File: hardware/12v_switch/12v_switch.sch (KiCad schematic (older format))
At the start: 51 parts, among them J1 MOLEX_0530470810, M1 SCREW_6-32_POWER, M11 SCREW_6-32_POWER, M12 SCREW_6-32_POWER, M13 SCREW_6-32_POWER, M14 SCREW_6-32_POWER, M19 SCREW_6-32_NORMAL, M2 SCREW_6-32_POWER, M20 SCREW_6-32_NORMAL, M21 SCREW_6-32_NORMAL, M22 SCREW_6-32_NORMAL, M3 SCREW_6-32_POWER, M4 SCREW_6-32_POWER, M5 SCREW_6-32_POWER, M6 SCREW_6-32_POWER, Q1 INFINEON_IRF7470TRPBF, Q2 INFINEON_IRF7470TRPBF, Q3 INFINEON_IRF7470TRPBF, Q4 INFINEON_IRF7470TRPBF, U1 TI_LM5111-1MX_NOPB, U2 TI_LM5111-1MX_NOPB, U3 TI_LM22680QMRE-ADJ

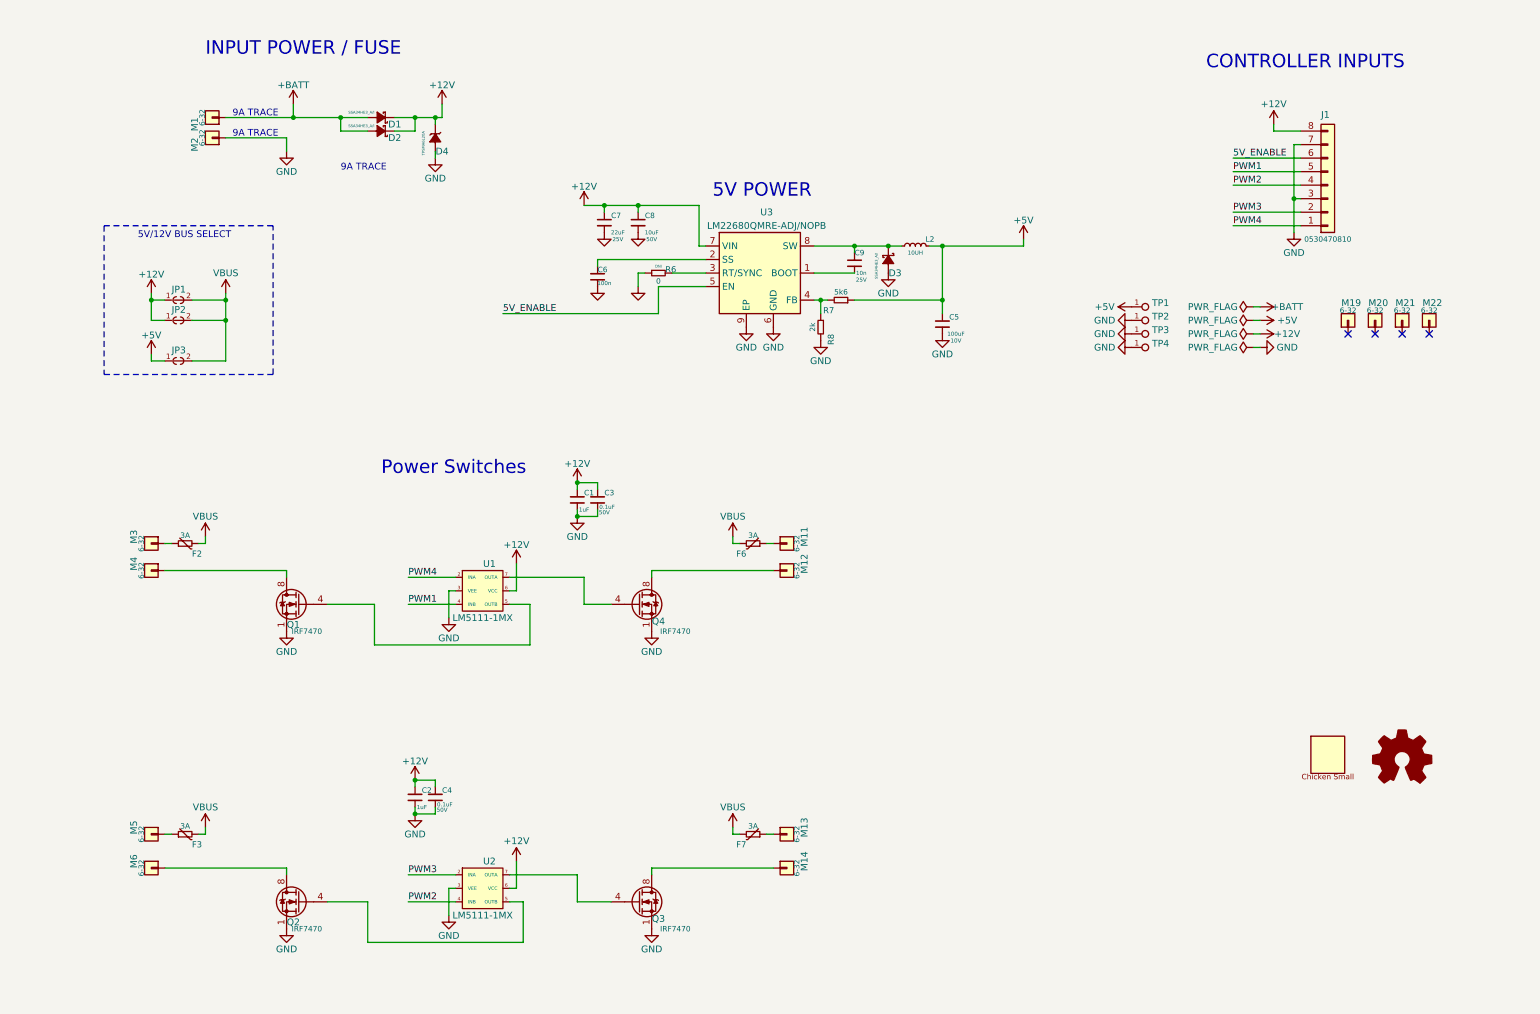
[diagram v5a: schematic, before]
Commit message: Added separate 5V gate driver LDO
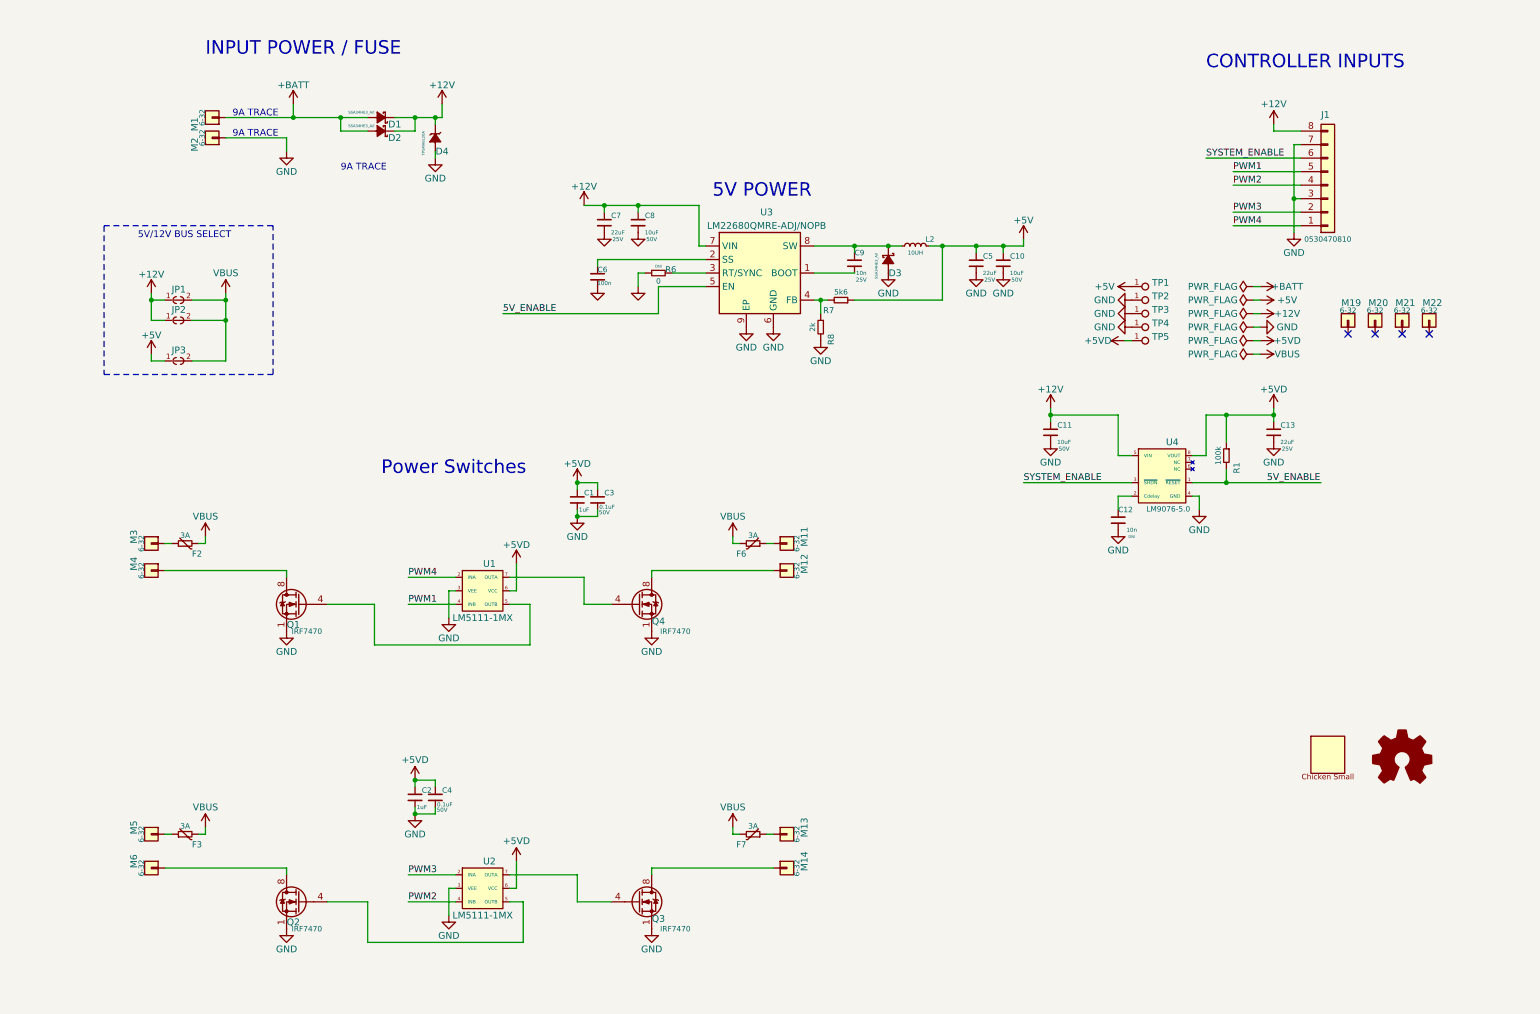
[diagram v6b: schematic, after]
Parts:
- removed C5: TAIYO-YUDEN_LMK325ABJ107MM-P, Capacitors_SMD:C_1210, symbol DBLS_Capacitor:TAIYO-YUDEN_LMK325ABJ107MM-P
- added C10, C11: MURATA_GRT31CR61H106KE01L, Capacitors_SMD:C_1206, symbol DBLS_Capacitor:MURATA_GRT31CR61H106KE01L
- added C12: MURATA_GCM155R71E103KA37D, Capacitors_SMD:C_0402, symbol DBLS_Capacitor:MURATA_GCM155R71E103KA37D
- added C13, C5: MURATA_GRM31CC81E226KE11L, Capacitors_SMD:C_1206, symbol DBLS_Capacitor:MURATA_GRM31CC81E226KE11L
- added R1: VISHAYDALE_CRCW0402100KJNEDC, Resistors_SMD:R_0402, symbol DBLS_Resistor:VISHAYDALE_CRCW0402100KJNEDC
- added TP5: DBLS_TESTPOINT_NORMAL, DBLS_Misc:DBLS_Testpoint_Normal, symbol DBLS_Misc:DBLS_TESTPOINT_NORMAL
- added U4: TI_LM9076BMA-5.0, Housings_SOIC:SOIC-8_3.9x4.9mm_Pitch1.27mm, symbol DBLS_LDO:TI_LM9076BMA-5.0
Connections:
- net +12V: now also C11.1, U4.5 (VIN); no longer C1.1, C2.1, C3.1, C4.1, U1.6 (VCC), U2.6 (VCC)
- net +5V: now also C10.1, C5.1
- net 5V_ENABLE: now also R1.2, U4.1 (~RESET); no longer J1.6 (Pin_6)
- net GND: now also C10.2, C11.2, C12.2, C13.2, C5.2, U4.4 (GND)
- new net: C12.1, U4.2 (Cdelay)
- new net +5VD: C1.1, C13.1, C2.1, C3.1, C4.1, R1.1, TP5.1, U1.6 (VCC), U2.6 (VCC), U4.8 (VOUT)
- new net SYSTEM_ENABLE: J1.6 (Pin_6), U4.3 (~SHDN)
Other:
- moved on the sheet: TP1, TP2, TP3, TP4

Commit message: added cad files for FreeCAD 0.19
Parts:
- removed C6: MURATA_GCM155R71C104KA55J, Capacitors_SMD:C_0402, symbol DBLS_Capacitor:MURATA_GCM155R71C104KA55J
- added C6: MURATA_GRM155R71H104ME14J, Capacitors_SMD:C_0402, symbol DBLS_Capacitor:MURATA_GRM155R71H104ME14J
- added LOGO2: DBLS_Chicken_Large, DBLS_LOGO:Rooster_43mmx43mm, symbol DBLS_Logo:DBLS_Chicken_Large
- added LOGO4: DBLS_van_logo_small_v1, DBLS_LOGO:van_logo_small, symbol DBLS_Logo:DBLS_van_logo_small_v1
- D1, D2, D3: PLACE YES -> (none)
- D4: PLACE YES -> (none); place (none) -> YES
- M11, M12, M13, M14, M3, M4, M5, M6: PLACE DNI -> (none); place (none) -> DNI
- U3: description (none) -> IC REG LINEAR 5V 150MA 8SOIC
- U4: symbol DBLS_LDO:TI_LM9076BMA-5.0 -> 12v_switch-rescue:TI_LM9076BMA-5.0-DBLS_LDO
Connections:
- net GND: now also C6.2
- net at U3.2 (SS): now also C6.1
